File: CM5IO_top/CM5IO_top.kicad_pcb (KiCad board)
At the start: 2 copper layers, 59.7 x 56.3 mm, 55 parts, among them J1 USB_C_Receptacle_USB2.0, J10 J_DShot600_FC, J3 J_PSU_EN, J4 J_ESP_DBG_UART, J7 J_FC_UART, J8 THD-20-R, J9 J_DShot600_ESC, Q1 AO3401A, Q2 Q_NPN_BEC, Q3 Q_NPN_BEC, Q4 AO3401A, SW1 SW_RESET, SW2 SW_BOOT, SW3 FORCE_PWR, U1 ESP32-S3-WROOM-1, U2 AP7361C-33E, U3 AP7361C-33E, U4 Waveshare Core1262 SX1262

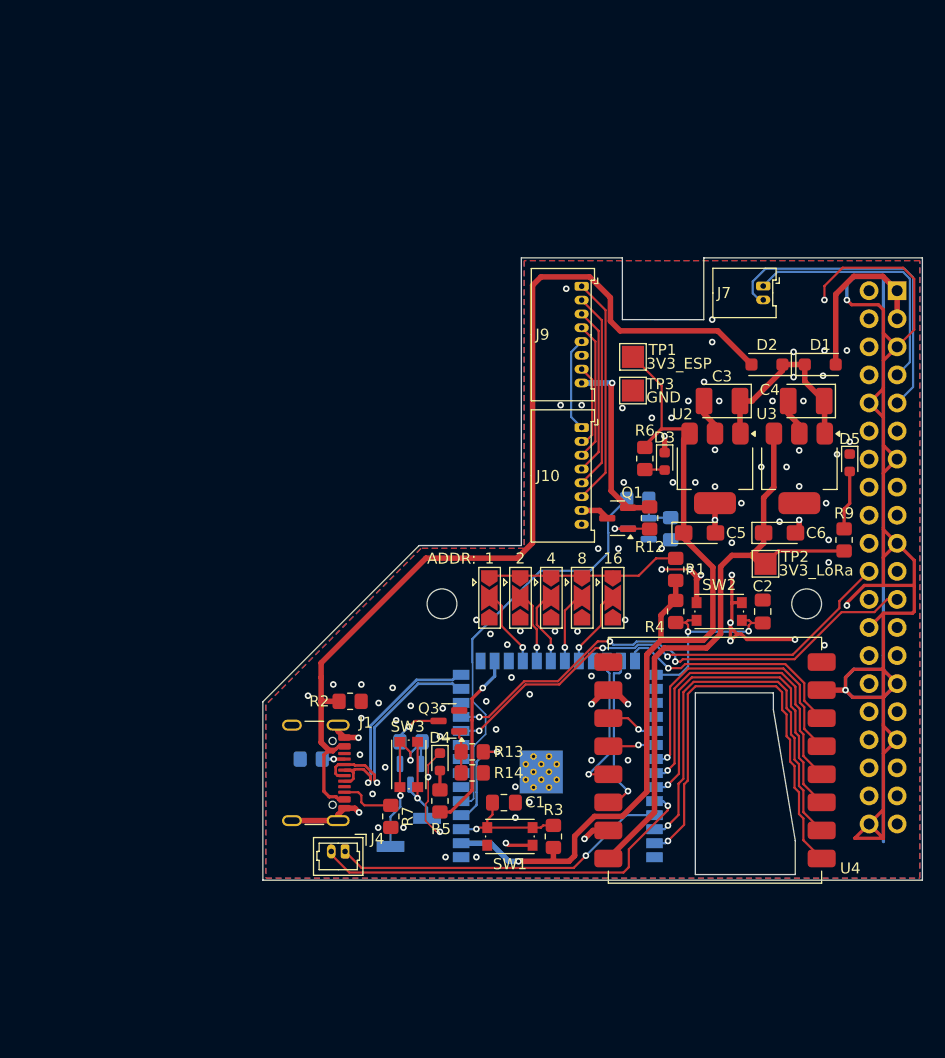
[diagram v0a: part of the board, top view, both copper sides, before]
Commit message: redesigning upper board
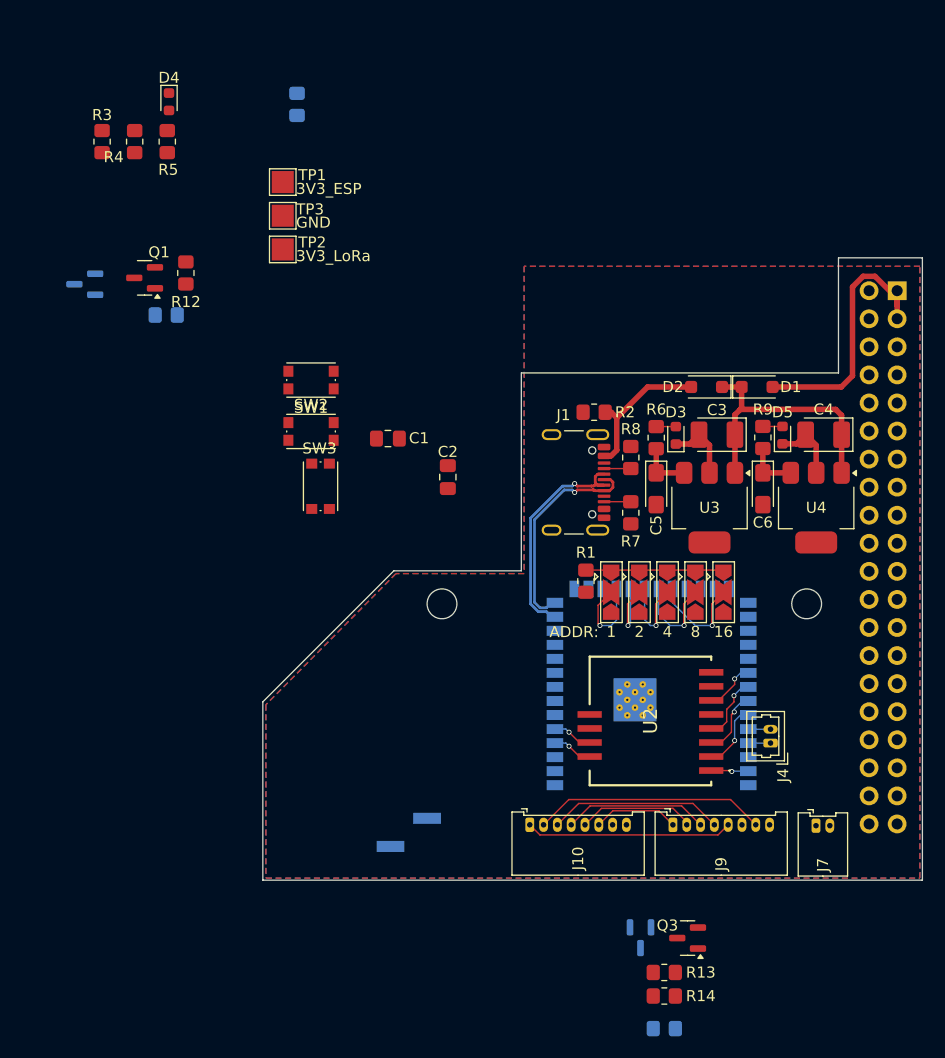
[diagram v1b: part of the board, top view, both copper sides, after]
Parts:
- removed the U4 at (187.2, 135.7)
- added U2: Wio-SX1262, CM5IO_top:Wio-SX1262, F.Cu at (181.4, 132.1)
- R8: moved to F.Cu
- U1: footprint RF_Module:ESP32-S3-WROOM-1 -> RF_Module:ESP32-S3-WROOM-1U
- moved R3 75.0 mm to (131.7, 79.7)
- moved R4 64.9 mm to (134.7, 79.7)
- moved D4 64.6 mm to (137.8, 76.1)
- moved R5 64.6 mm to (137.6, 79.7)
- moved Q2 54.8 mm to (130.2, 92.6)
- moved TP2 52.1 mm to (148.1, 89.4)
- moved R11 51.2 mm to (149.4, 76.3)
- moved J9 49.4 mm to (183.4, 141.5), turned to 0 degrees
- moved J7 49.1 mm to (196.3, 141.6), turned to 0 degrees
- moved Q1 48.0 mm to (135.6, 92.0)
- moved R12 47.5 mm to (139.3, 91.6)
- moved R10 45.8 mm to (137.5, 95.4)
- moved SW1 45.1 mm to (150.6, 101.3)
- moved SW2 40.4 mm to (150.6, 105.9)
- moved R8 39.8 mm to (179.6, 108.3), turned to -90 degrees
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- renumbered U2 to U3, U3 to U4
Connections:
- U1 pad 24: /Comm/LORA_DIO2 -> unconnected-(U1-IO47-Pad24)
- U1 pad 25: /Comm/LORA_DIO1 -> unconnected-(U1-IO48-Pad25)
- U1 pad 26: /Comm/LORA_SPI_CS -> unconnected-(U1-IO45-Pad26)
- U1 pad 31: /Comm/LORA_RXEN -> unconnected-(U1-IO38-Pad31)
- U1 pad 32: /Comm/LORA_TXEN -> /Comm/LORA_SPI_CS
- U1 pad 38: /Comm/LORA_RESET -> unconnected-(U1-IO2-Pad38)
- U1 pad 39: /Comm/LORA_BUSY -> /Comm/LORA_RF_SW
- U1 pad 4: /Comm/KILLSWITCH_PSU_CTL -> /Comm/LORA_DIO1
- U1 pad 5: /Comm/KILLSWITCH_FC_CTL -> /Comm/LORA_BUSY
- U1 pad 6: unconnected-(U1-IO6-Pad6) -> /Comm/KILLSWITCH_PSU_CTL
- U1 pad 7: unconnected-(U1-IO7-Pad7) -> /Comm/KILLSWITCH_FC_CTL
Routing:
- net GND: track 254.8 -> 13.1 mm, vias 97 -> 0
- net /+5v_USB: track 90.0 -> 13.4 mm
- net /+3.3v_ESP: track 79.5 -> 4.71 mm, vias 1 -> 0
- net /+3.3v_LoRa: track 57.1 -> 4.73 mm
- net /GPIO8: track 46.0 -> 0.00 mm, vias 3 -> 0
- net /GPIO9: track 44.2 -> 0.00 mm, vias 3 -> 0
- net /Comm/LORA_RESET: track 38.0 -> 0.00 mm, vias 1 -> 0
- net /Comm/KILLSWITCH_FC_CTL: track 37.7 -> 0.00 mm
- net /Comm/LORA_BUSY: track 40.9 -> 3.65 mm
- net Net-(J4-Pin_2): track 36.2 -> 2.02 mm, vias 1 -> 0
- net /GPIO15_UART_RX: track 29.5 -> 0.00 mm
- net Net-(J4-Pin_1): track 30.9 -> 2.01 mm, vias 1 -> 0
- net /Comm/LORA_SPI_MISO: track 32.8 -> 6.02 mm
- net /Comm/LORA_SPI_MOSI: track 29.9 -> 5.98 mm
- net /GPIO14_UART_TX: track 23.2 -> 0.00 mm
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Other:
- outline, holes or cut-outs redrawn

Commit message: top board wip
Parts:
- Q1, R12: moved to B.Cu
- Q4, R15: moved to F.Cu
- moved R11 78.1 mm to (187.8, 144.3)
- moved Q2 75.3 mm to (184.9, 144.3)
- moved R10 71.6 mm to (190.7, 143.3), turned to 180 degrees
- moved R3 69.0 mm to (171.4, 136.2), turned to 0 degrees
- moved Q1 67.9 mm to (178.9, 144.3)
- moved R12 67.8 mm to (181.9, 144.3), turned to 90 degrees
- moved SW1 35.6 mm to (171.1, 130.3), turned to 90 degrees
- moved SW3 32.3 mm to (159.5, 142.2)
- moved C1 30.8 mm to (171.4, 134.1), turned to 0 degrees
- moved R4 28.4 mm to (146.1, 105.7)
- moved Q3 24.2 mm to (163.3, 140.5)
- moved R14 23.2 mm to (166.4, 140.4), turned to 90 degrees
- moved R15 22.6 mm to (166.4, 144.2), turned to 90 degrees
- moved R13 22.1 mm to (168.4, 137.9), turned to -90 degrees
- moved Q4 18.7 mm to (163.3, 144.2), turned to 0 degrees
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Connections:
- U1 pad 38: unconnected-(U1-IO2-Pad38) -> /Comm/LORA_RF_SW
- U1 pad 39: /Comm/LORA_RF_SW -> /Comm/KILLSWITCH_FC_CTL
- U1 pad 7: /Comm/KILLSWITCH_FC_CTL -> unconnected-(U1-IO7-Pad7)
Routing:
- net /GPIO14_UART_TX: track 0.00 -> 53.5 mm
- net /GPIO15_UART_RX: track 0.00 -> 49.7 mm
- net /VBUS_ESC: track 0.00 -> 16.7 mm, vias 0 -> 1
- net /PSU_VIN: track 0.00 -> 13.7 mm, vias 0 -> 1
- net /PSU_CTL_EN: track 0.00 -> 9.77 mm, vias 0 -> 1
- net /Comm/KILLSWITCH_FC_CTL: track 0.00 -> 9.21 mm
- net Net-(Q3-C): track 0.00 -> 6.55 mm
- net /Comm/ENABLE: track 0.00 -> 6.40 mm, vias 0 -> 1
- net Net-(Q3-B): track 0.00 -> 6.09 mm
- net GND: track 13.1 -> 18.4 mm, vias 0 -> 5
- net Net-(Q1-G): track 0.00 -> 4.60 mm
- net Net-(Q2-B): track 0.00 -> 3.91 mm
- net /+3.3v_ESP: track 4.71 -> 8.31 mm, vias 0 -> 1
- net /VBUS_FC: track 0.00 -> 2.79 mm

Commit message: upper board finished (I hope)
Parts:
- added C7: 470nF, Capacitor_SMD:C_0805_2012Metric_Pad1.18x1.45mm_HandSolder, B.Cu at (174.9, 139.5)
- added C8: 470nF, Capacitor_SMD:C_0805_2012Metric_Pad1.18x1.45mm_HandSolder, F.Cu at (193.7, 128.0)
- added R16: 10K, Resistor_SMD:R_0805_2012Metric_Pad1.20x1.40mm_HandSolder, B.Cu at (164.2, 141.6)
- C3, C4: value 4.7uF 25v -> 4.7uF 35v
- C5, C6: value 4.7uF 6.3v -> 4.7uF 10v
- J3: footprint Connector_PinHeader_2.54mm:PinHeader_1x02_P2.54mm_Vertical_SMD_Pin1Left -> Connector_PinSocket_2.54mm:PinSocket_1x02_P2.54mm_Vertical_SMD_Pin1Left
- J4: footprint Connector_Molex:Molex_PicoBlade_53047-0210_1x02_P1.25mm_Vertical -> Connector_Molex:Molex_PicoBlade_53047-0310_1x03_P1.25mm_Vertical
- J8: footprint Connector_PinHeader_2.54mm:PinHeader_2x20_P2.54mm_Vertical -> Connector_PinSocket_2.54mm:PinSocket_2x20_P2.54mm_Vertical
- R13, R5, R7, TP1, TP2, TP3: moved to B.Cu
- moved D4 79.7 mm to (198.8, 127.5), turned to 90 degrees
- moved R5 72.7 mm to (193.1, 126.7), turned to 0 degrees
- moved TP3 53.4 mm to (192.2, 116.4), turned to 180 degrees
- moved TP2 50.2 mm to (192.2, 113.3), turned to 180 degrees
- moved TP1 42.9 mm to (182.0, 109.6), turned to 180 degrees
- moved SW2 33.6 mm to (174.6, 129.4), turned to 180 degrees
- moved R4 33.6 mm to (173.8, 124.6), turned to 0 degrees
- moved C2 27.9 mm to (173.7, 126.6), turned to 0 degrees
- moved R8 7.70 mm to (173.7, 103.3)
- moved SW1 4.41 mm to (174.6, 133.0), turned to 0 degrees
- moved U2 3.88 mm to (185.1, 133.2)
- moved J4 3.12 mm to (195.3, 134.5)
- moved R3 2.96 mm to (173.8, 137.9)
- moved C1 2.96 mm to (173.7, 135.9)
- moved R13 2.74 mm to (167.3, 140.4)
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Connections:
- J4 pad 1: Net-(J4-Pin_1) -> GND
- J8 pad 1: /+5v_RPi -> unconnected-(J8-Pin_1-Pad1)
- J8 pad 10: GND -> /GPIO15_UART_RX
- J8 pad 11: /GPIO18 -> /GPIO17
- J8 pad 12: /GPIO17 -> /GPIO18
- J8 pad 13: GND -> /GPIO27
- J8 pad 14: /GPIO27 -> GND
- J8 pad 15: /GPIO23 -> /GPIO22
- J8 pad 16: /GPIO22 -> /GPIO23
- J8 pad 17: /GPIO24 -> unconnected-(J8-Pin_17-Pad17)
- J8 pad 18: unconnected-(J8-Pin_18-Pad18) -> /GPIO24
- J8 pad 19: GND -> /GPIO10
- J8 pad 2: unconnected-(J8-Pin_2-Pad2) -> /+5v_RPi
- J8 pad 20: /GPIO10 -> GND
- J8 pad 21: /GPIO25 -> /GPIO9
- J8 pad 22: /GPIO9 -> /GPIO25
- J8 pad 23: /GPIO8 -> /GPIO11
- J8 pad 24: /GPIO11 -> /GPIO8
- J8 pad 25: /GPIO7 -> GND
- J8 pad 26: GND -> /GPIO7
- J8 pad 29: GND -> /GPIO5
- J8 pad 3: /+5v_RPi -> /GPIO2
- J8 pad 30: /GPIO5 -> GND
- J8 pad 31: /GPIO12 -> /GPIO6
- J8 pad 32: /GPIO6 -> /GPIO12
- J8 pad 33: GND -> /GPIO13
- J8 pad 34: /GPIO13 -> GND
- J8 pad 35: /GPIO16 -> /GPIO19
- J8 pad 36: /GPIO19 -> /GPIO16
- J8 pad 37: /GPIO20 -> /GPIO26
- J8 pad 38: /GPIO26 -> /GPIO20
- J8 pad 39: /GPIO21 -> GND
- J8 pad 4: /GPIO2 -> /+5v_RPi
- J8 pad 40: GND -> /GPIO21
- J8 pad 5: GND -> /GPIO3
- J8 pad 6: /GPIO3 -> GND
- J8 pad 7: /GPIO14_UART_TX -> /GPIO4
- J8 pad 8: /GPIO4 -> /GPIO14_UART_TX
- J8 pad 9: /GPIO15_UART_RX -> GND
- U1 pad 16: /Comm/LED_ACT -> unconnected-(U1-IO46-Pad16)
- U1 pad 26: unconnected-(U1-IO45-Pad26) -> /Comm/LED_ACT
- U1 pad 31: unconnected-(U1-IO38-Pad31) -> /Comm/LORA_SPI_CS
- U1 pad 32: /Comm/LORA_SPI_CS -> /Comm/LORA_RESET
- U1 pad 36: Net-(J4-Pin_2) -> Net-(J4-Pin_3)
- U1 pad 37: Net-(J4-Pin_1) -> Net-(J4-Pin_2)
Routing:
- net /+3.3v_ESP: track 8.31 -> 57.7 mm, vias 1 -> 2
- net /GPIO8: track 0.00 -> 33.7 mm, vias 0 -> 2
- net /GPIO9: track 0.00 -> 32.1 mm, vias 0 -> 2
- net /Comm/BOOT_MODE: track 0.00 -> 27.4 mm, vias 0 -> 1
- net /+3.3v_LoRa: track 4.73 -> 31.0 mm, vias 0 -> 1
- net GND: track 18.4 -> 44.0 mm, vias 5 -> 60
- net /Comm/KILLSWITCH_PSU_CTL: track 0.00 -> 12.2 mm
- net /Comm/LORA_RESET: track 0.00 -> 11.0 mm, vias 0 -> 1
- net /Comm/LED_ACT: track 0.00 -> 10.2 mm
- net /+5v_USB: track 13.4 -> 22.9 mm
- net /Comm/LORA_SPI_CS: track 4.68 -> 12.0 mm
- net /PSU_CTL_EN: track 9.77 -> 15.0 mm
- net Net-(J4-Pin_3): track 0.00 -> 5.12 mm
- net /Comm/ENABLE: track 6.40 -> 11.3 mm
- net Net-(J1-CC1): track 2.42 -> 7.27 mm
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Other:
- board size 59.7 x 56.3 mm -> 50.3 x 56.3 mm
- board text added: "39"
- board text added: "40"
- board text added: "ADDR SEL"
- board text added: "BOOT"
- board text added: "CM5IO drone board IARC Hat"
- board text added: "DBG UART"
- board text added: "ESC DSHOT"
- board text added: "FC"
- board text added: "FC DSHOT"
- board text added: "LED ACT"
- board text added: "LED PWR ESP32"
- board text added: "LED PWR SX1262"
- board text added: "PSU_EN"
- board text added: "RST"
- board text added: "Solder 10K to disable PSU autostart"
- board text added: "rev. 1.0, 01.2026"
- board text removed: "ADDR:"
- board text removed: "Board thickness : 1.6mm Finished copper weight inners : 24.9um or greater Finished copper weight outers : 35um or greater Board finish : OSP Material type : FR4 Colour of solder resists : Green Colour of silk screens : White Only on the top side Board to : UL94-V0 TG >=130 50R trace width 0.13mm@ 3GHz 90R diff pair width 0.147 spacing 0.253mm @ 2.5GHz 100R diff pair width 0.127 spacing 0.253mm @ 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"
